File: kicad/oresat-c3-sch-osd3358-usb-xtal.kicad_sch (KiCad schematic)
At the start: 36 parts, among them U1 OSD3358-512M-BSM, U11 RCLAMP0504FB, Y1 24MHz, Y2 Crystal

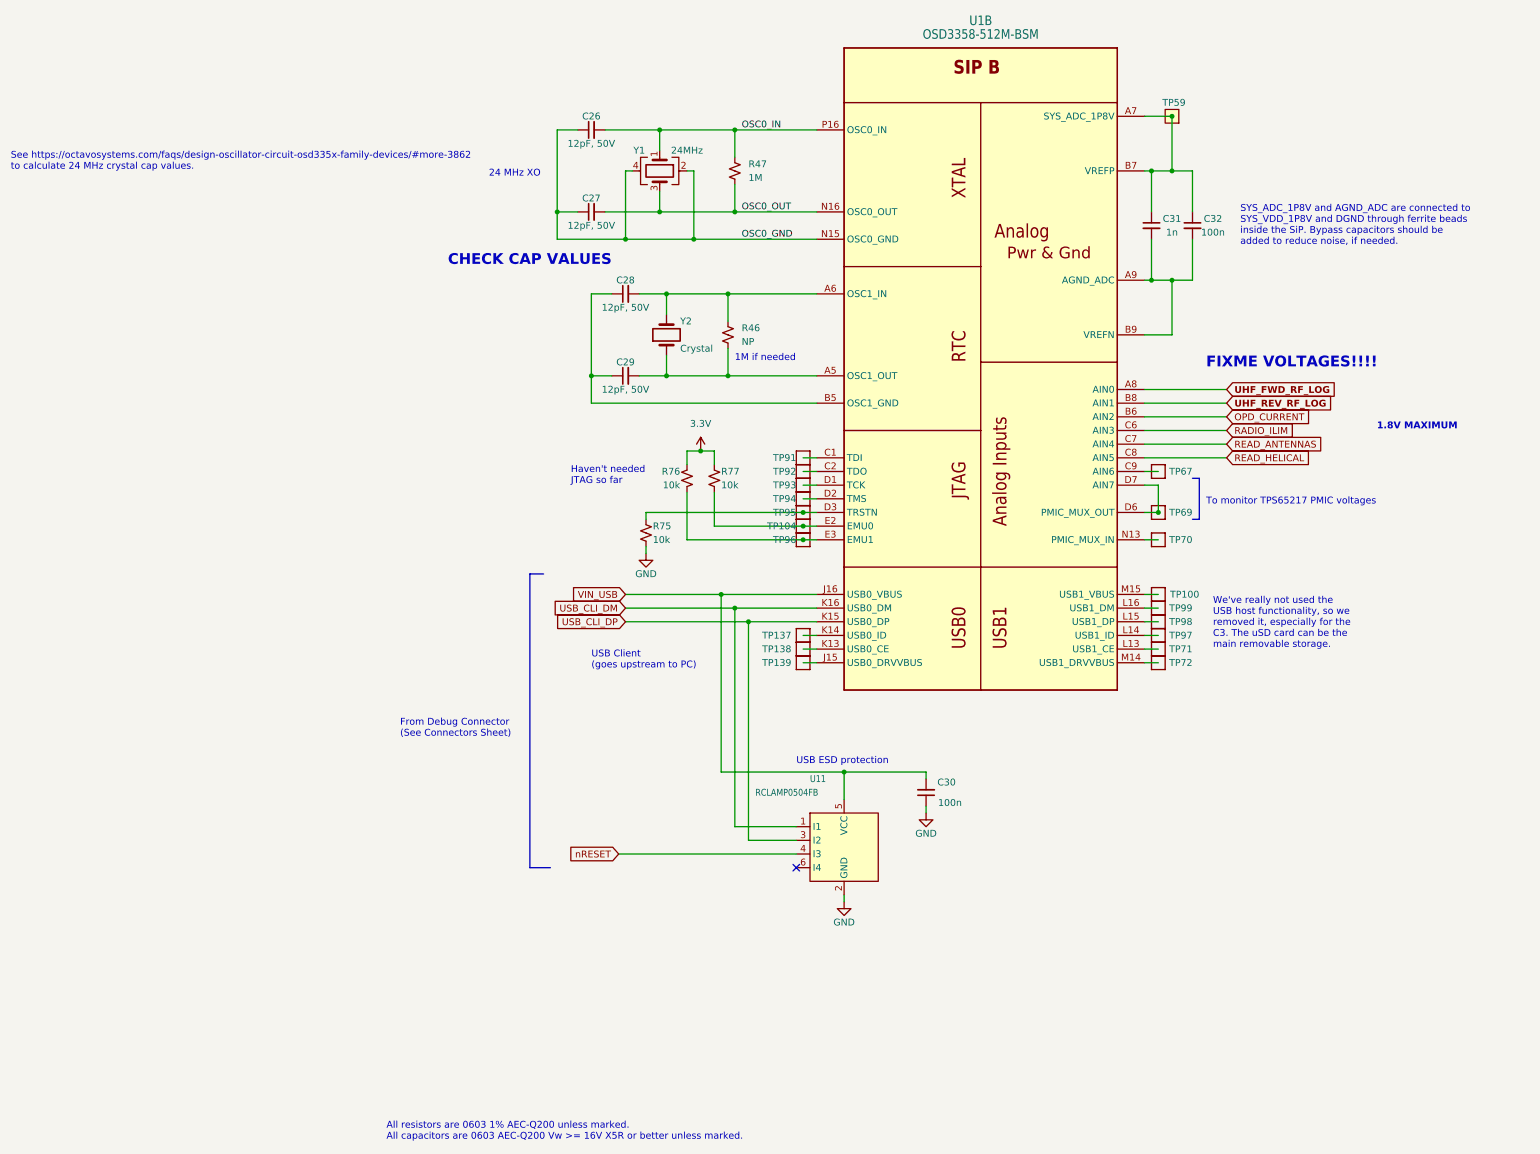
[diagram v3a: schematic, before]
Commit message: Added reset states of GPIO lines to OSD3358 pins in schematic so we know what pulls up unexpectedly. Re-arranged a few pins that should not pull up on boot.
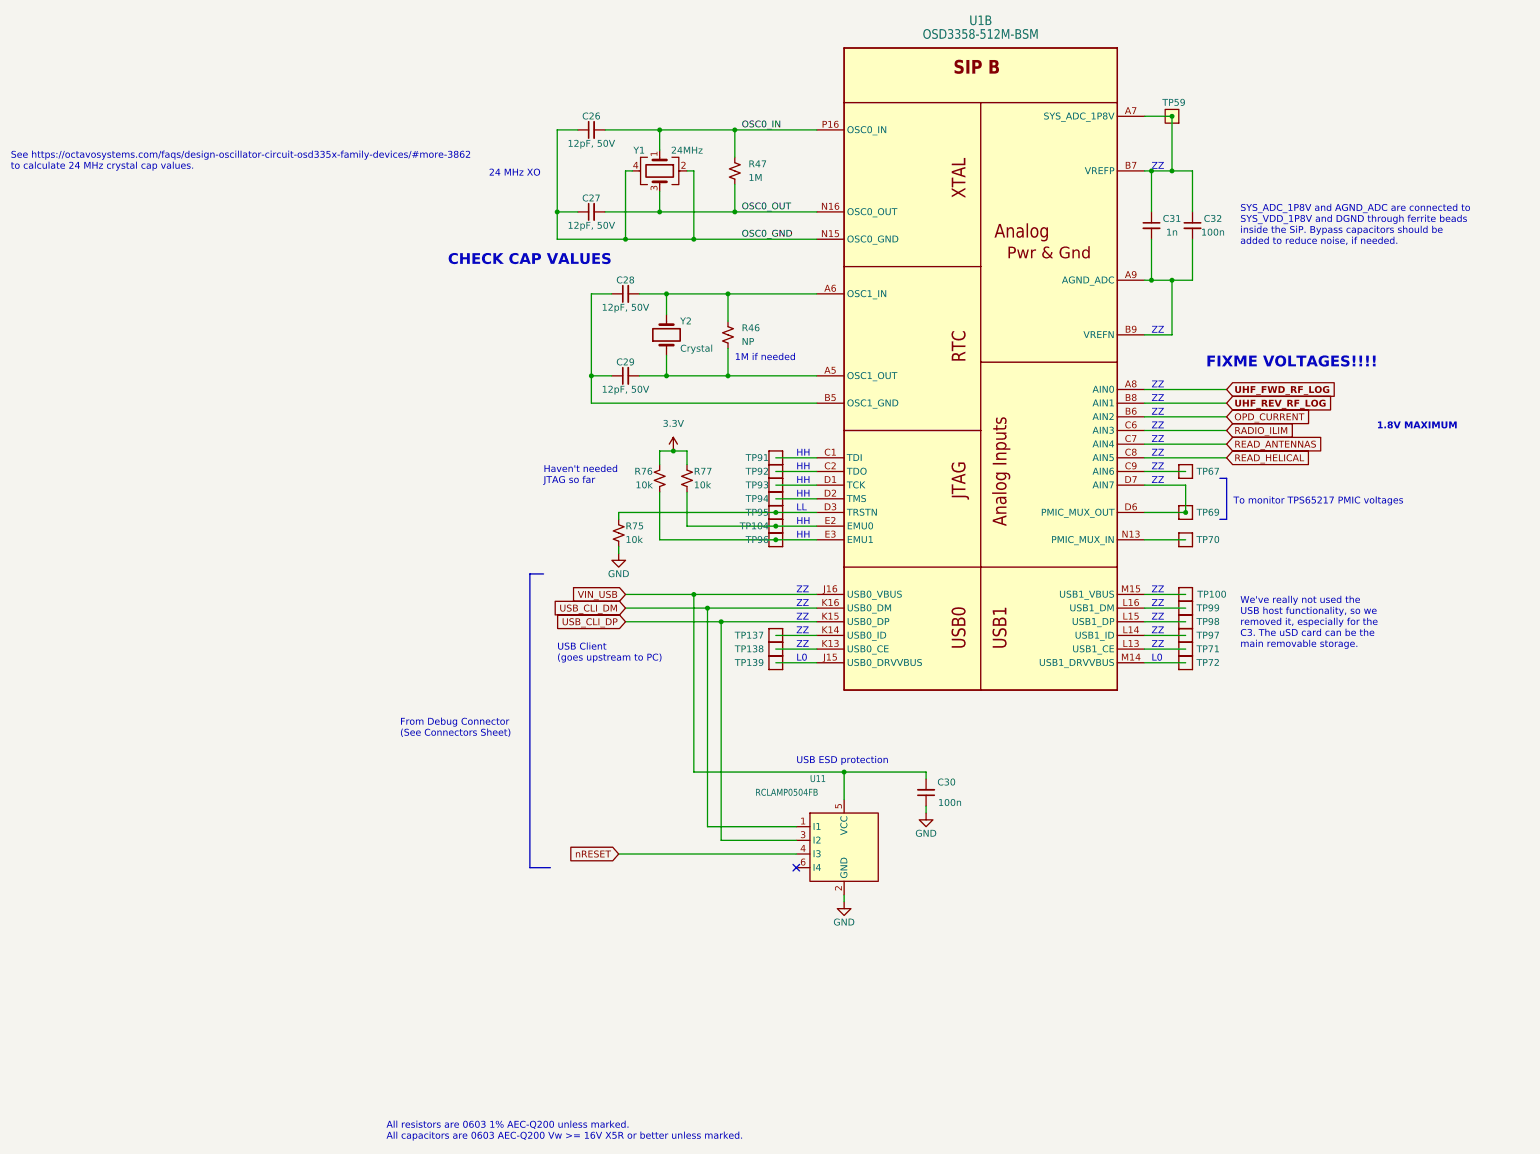
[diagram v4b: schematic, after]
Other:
- note added: "HH"
- note added: "L0"
- note added: "LL"
- note added: "ZZ"
- moved on the sheet: R75, R76, R77, TP100, TP104, TP137, TP138, TP139, TP67, TP69, TP70, TP71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

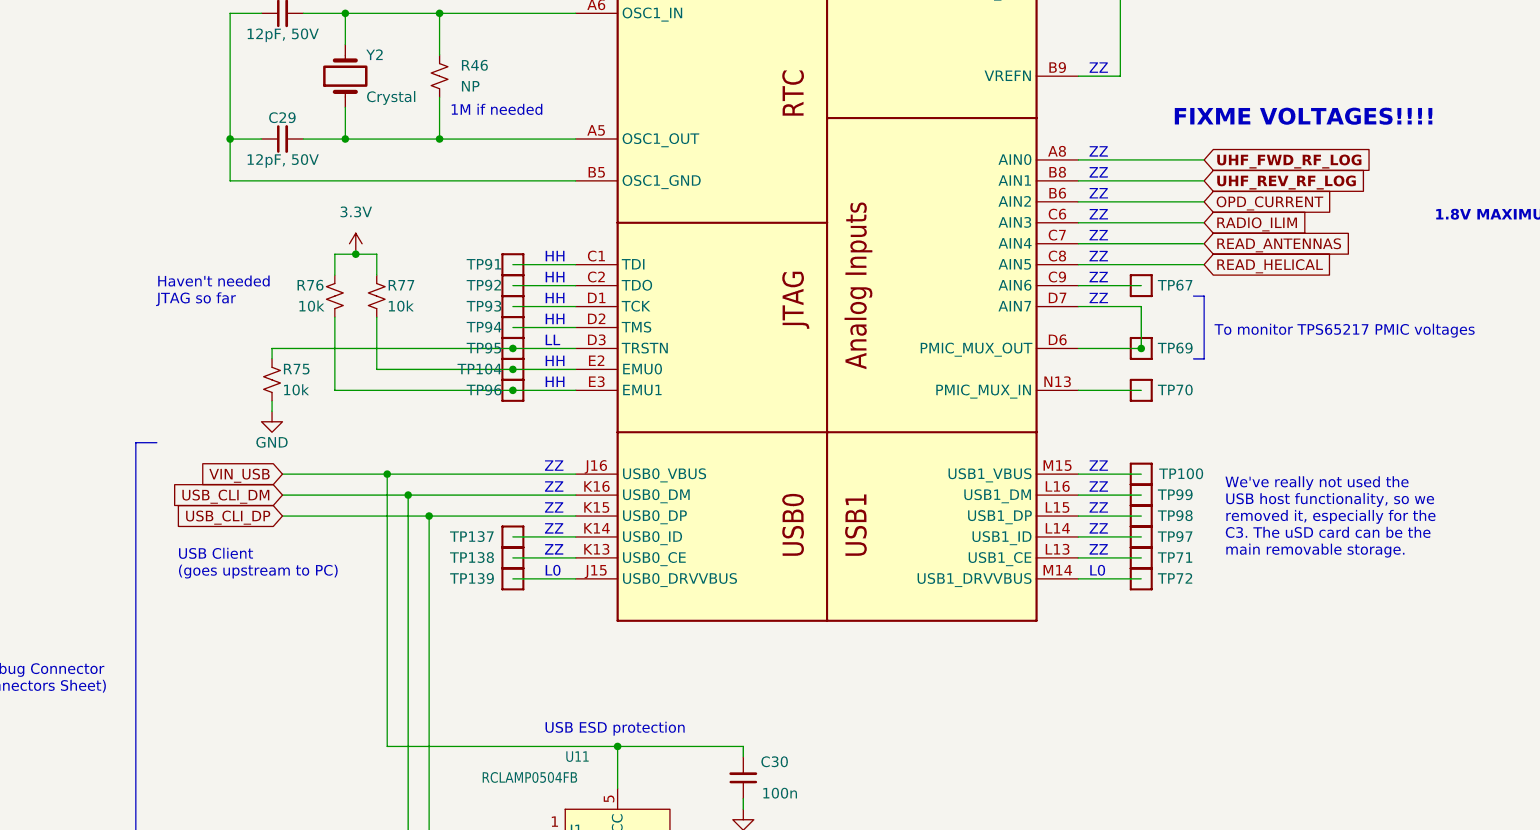
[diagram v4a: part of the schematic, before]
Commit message: An evening of cleanups from the design review. Includes lots of ERC and DRC cleanup, although still over 450 DRC errors mostly from RF keepouts. Fixed PA ground connection, notes on pin reset configuration, and lots of small naggy things. Also cleaned up wierd broken traces on eMMC traces. No longer all same length (sorry Oliver) but it shouldn't affect performance.
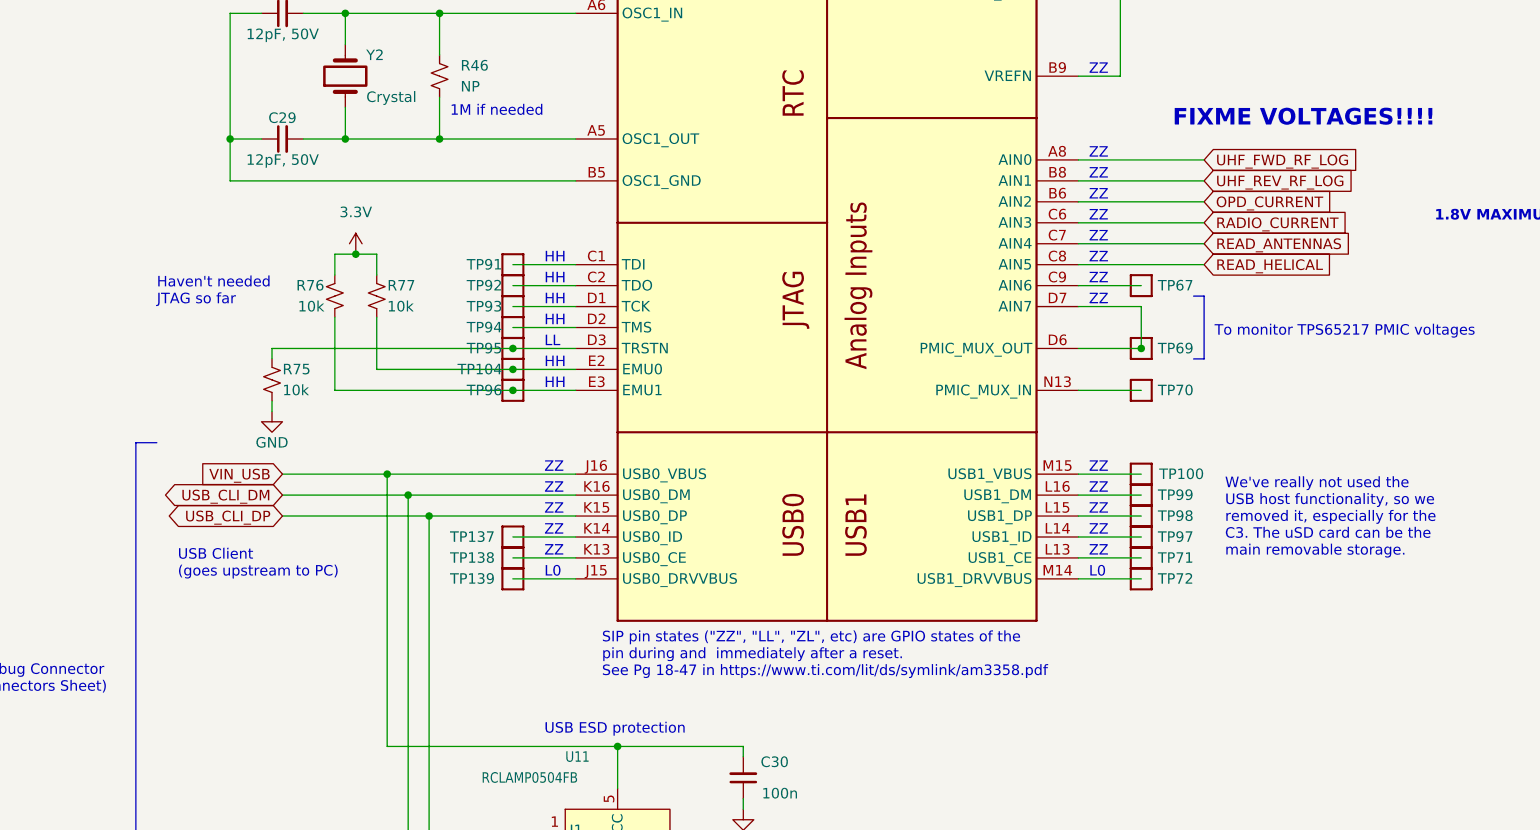
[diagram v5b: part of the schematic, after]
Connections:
- net RADIO_ILIM renamed RADIO_CURRENT
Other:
- note added: "SIP pin states ("ZZ", "LL", "ZL", etc) are GPIO states of the pin during and immediately after a reset. See Pg 18-47 in https://www.ti.com/lit/ds/symlink/am3358.pdf"
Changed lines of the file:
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@@
+    (effects (font (size 1.27 1.27)) (justify left bottom))
+  )
+  (text "SIP pin states (\"ZZ\", \"LL\", \"ZL\", etc) are GPIO states of the\npin during and  immediately after a reset.  \nSee Pg 18-47 in https://www.ti.com/lit/ds/symlink/am3358.pdf\n"
+    (at 198.755 184.785 0)
     (effects (font (size 1.27 1.27)) (justify left bottom))
   )
@@
     (effects (font (size 1.2446 1.2446)) (justify left bottom))
   )
-  (global_label "USB_CLI_DP" (shape input) (at 160.02 165.1 180)
+  (global_label "USB_CLI_DP" (shape bidirectional) (at 160.02 165.1 180)
     (effects (font (size 1.27 1.27)) (justify right))
     (property "Intersheetrefs" "${INTERSHEET_REFS}" (at 146.05 165.1 0)
@@
     )
   )
-  (global_label "USB_CLI_DM" (shape input) (at 160.02 162.56 180)
+  (global_label "USB_CLI_DM" (shape bidirectional) (at 160.02 162.56 180)
     (effects (font (size 1.27 1.27)) (justify right))
     (property "Intersheetrefs" "${INTERSHEET_REFS}" (at 146.05 162.56 0)
@@
   )
   (global_label "UHF_FWD_RF_LOG" (shape input) (at 271.78 121.92 0) (fields_autoplaced)
-    (effects (font (size 1.27 1.27) (thickness 0.254) bold) (justify left))
-    (property "Intersheetrefs" "${INTERSHEET_REFS}" (at 291.5638 121.92 0)
+    (effects (font (size 1.27 1.27)) (justify left))
+    (property "Intersheetrefs" "${INTERSHEET_REFS}" (at 291.1354 121.92 0)
       (effects (font (size 1.27 1.27)) (justify left))
     )
@@
   )
   (global_label "UHF_REV_RF_LOG" (shape input) (at 271.78 124.46 0) (fields_autoplaced)
-    (effects (font (size 1.27 1.27) (thickness 0.254) bold) (justify left))
-    (property "Intersheetrefs" "${INTERSHEET_REFS}" (at 291.2614 124.46 0)
+    (effects (font (size 1.27 1.27)) (justify left))
+    (property "Intersheetrefs" "${INTERSHEET_REFS}" (at 290.833 124.46 0)
       (effects (font (size 1.27 1.27)) (justify left))
     )
@@
     )
   )
-  (global_label "RADIO_ILIM" (shape input) (at 271.78 129.54 0) (fields_autoplaced)
+  (global_label "RADIO_CURRENT" (shape input) (at 271.78 129.54 0) (fields_autoplaced)
     (effects (font (size 1.27 1.27)) (justify left))
-    (property "Intersheetrefs" "${INTERSHEET_REFS}" (at 284.9064 129.54 0)
+    (property "Intersheetrefs" "${INTERSHEET_REFS}" (at 289.8049 129.54 0)
       (effects (font (size 1.27 1.27)) (justify left))
     )

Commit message: Last of the ERC and DRC errors! only polishing left.
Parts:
- U1: footprint oresat-footprints:U-Octavo-OSD335X-BGA-256 -> oresat-ics:U-Octavo-OSD335X-BGA-256
- Y1: footprint oresat-footprints:CRYSTAL-5X3.2-4SMD -> oresat-passives:CRYSTAL-5X3.2-4SMD
- Y2: footprint oresat-footprints:CRYSTAL_3.2X1.5 -> oresat-passives:CRYSTAL_3.2X1.5
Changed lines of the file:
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@@
       (effects (font (size 1.27 1.27)))
     )
-    (property "Footprint" "oresat-footprints:CRYSTAL-5X3.2-4SMD" (at 166.37 81.28 0)
+    (property "Footprint" "oresat-passives:CRYSTAL-5X3.2-4SMD" (at 166.37 81.28 0)
       (effects (font (size 1.27 1.27)) hide)
     )
@@
       (effects (font (size 1.27 1.27)) (justify right))
     )
-    (property "Footprint" "oresat-footprints:CRYSTAL_3.2X1.5" (at 167.64 111.76 0)
+    (property "Footprint" "oresat-passives:CRYSTAL_3.2X1.5" (at 167.64 111.76 0)
       (effects (font (size 1.27 1.27)) hide)
     )
@@
       (effects (font (size 1.778 1.5113)))
     )
-    (property "Footprint" "oresat-footprints:U-Octavo-OSD335X-BGA-256" (at 226.06 8.89 0)
-      (effects (font (size 1.27 1.27)) hide)
-    )
+    (property "Footprint" "oresat-ics:U-Octavo-OSD335X-BGA-256" (at 226.06 8.89 0)
+      (effects (font (size 1.27 1.27)) hide)
+    )
